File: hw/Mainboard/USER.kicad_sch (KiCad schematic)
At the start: 1 part, among them J4 USER

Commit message: hw: wip
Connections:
- net GND renamed PD_GND
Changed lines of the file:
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@@
+    (stroke (width 0) (type default) (color 0 0 0 0))
+  )
+  (wire (pts (xy 142.24 115.57) (xy 148.59 115.57))
     (stroke (width 0) (type default) (color 0 0 0 0))
   )
@@
   )
   (wire (pts (xy 167.64 85.09) (xy 167.64 86.36))
-    (stroke (width 0) (type default) (color 0 0 0 0))
-  )
-  (wire (pts (xy 142.24 115.57) (xy 148.59 115.57))
     (stroke (width 0) (type default) (color 0 0 0 0))
   )
@@
     (pin "N")
   )
-  (symbol (lib_id "power:GND") (at 115.57 86.36 0) (unit 1)
+  (symbol (lib_id "PET:PD_GND") (at 142.24 115.57 0) (unit 1)
     (in_bom yes) (on_board yes) (fields_autoplaced)
-    (property "Reference" "#PWR0117" (id 0) (at 115.57 92.71 0)
-      (effects (font (size 1.27 1.27)) hide)
-    )
-    (property "Value" "GND" (id 1) (at 115.57 91.44 0))
+    (property "Reference" "#PWR0117" (id 0) (at 142.24 121.92 0)
+      (effects (font (size 1.27 1.27)) hide)
+    )
+    (property "Value" "PD_GND" (id 1) (at 142.24 120.65 0))
+    (property "Footprint" "" (id 2) (at 142.24 115.57 0)
+      (effects (font (size 1.27 1.27)) hide)
+    )
+    (property "Datasheet" "" (id 3) (at 142.24 115.57 0)
+      (effects (font (size 1.27 1.27)) hide)
+    )
+    (pin "1")
+  )
+  (symbol (lib_id "PET:PD_GND") (at 115.57 86.36 0) (unit 1)
+    (in_bom yes) (on_board yes) (fields_autoplaced)
+    (property "Reference" "#PWR0121" (id 0) (at 115.57 92.71 0)
+      (effects (font (size 1.27 1.27)) hide)
+    )
+    (property "Value" "PD_GND" (id 1) (at 115.57 91.44 0))
     (property "Footprint" "" (id 2) (at 115.57 86.36 0)
       (effects (font (size 1.27 1.27)) hide)
@@
     (pin "1")
   )
-  (symbol (lib_id "power:GND") (at 167.64 86.36 0) (unit 1)
+  (symbol (lib_id "PET:PD_GND") (at 167.64 86.36 0) (unit 1)
     (in_bom yes) (on_board yes) (fields_autoplaced)
     (property "Reference" "#PWR0118" (id 0) (at 167.64 92.71 0)
       (effects (font (size 1.27 1.27)) hide)
     )
-    (property "Value" "GND" (id 1) (at 167.64 91.44 0))
+    (property "Value" "PD_GND" (id 1) (at 167.64 91.44 0))
     (property "Footprint" "" (id 2) (at 167.64 86.36 0)
       (effects (font (size 1.27 1.27)) hide)
@@
       (effects (font (size 1.27 1.27)) hide)
     )
-    (pin "1")
-  )
-  (symbol (lib_id "power:GND") (at 142.24 115.57 0) (unit 1)
-    (in_bom yes) (on_board yes) (fields_autoplaced)
-    (property "Reference" "#PWR0121" (id 0) (at 142.24 121.92 0)
-      (effects (font (size 1.27 1.27)) hide)
-    )
-    (property "Value" "GND" (id 1) (at 142.24 120.65 0))
-    (property "Footprint" "" (id 2) (at 142.24 115.57 0)
-      (effects (font (size 1.27 1.27)) hide)
-    )
-    (property "Datasheet" "" (id 3) (at 142.24 115.57 0)
-      (effects (font (size 1.27 1.27)) hide)
-    )

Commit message: hw: autoroute
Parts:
- added J26: USER_HEADER, Connector_PinHeader_2.54mm:PinHeader_2x11_P2.54mm_Vertical, symbol Connector_Generic:Conn_02x11_Odd_Even
- added PT26: PowerTie_2, PET:NetTie-2_SMD_Pad_1.6_to_0.4mm, symbol PET:PowerTie_2
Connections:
- net BHORIZ: now also J26.5 (Pin_5)
- net BVERT: now also J26.7 (Pin_7)
- net BVIDEO: now also J26.21 (Pin_21)
- net CASS1_READ: now also J26.9 (Pin_9)
- net CASS2_READ: now also J26.13 (Pin_13)
- net CASS_WRITE: now also J26.11 (Pin_11)
- net DIAG: now also J26.15 (Pin_15)
- net EOI: now also J26.17 (Pin_17)
- net GRAPHIC: now also J26.3 (Pin_3)
- net PD_GND: now also J26.1 (Pin_1)
- net SRQ: now also J26.19 (Pin_19)
- net VIA_CA1: now also J26.22 (Pin_22)
- net VIA_CB2: now also J26.4 (Pin_4)
- net VIA_PA0: now also J26.20 (Pin_20)
- net VIA_PA1: now also J26.18 (Pin_18)
- net VIA_PA2: now also J26.16 (Pin_16)
- net VIA_PA3: now also J26.14 (Pin_14)
- net VIA_PA4: now also J26.12 (Pin_12)
- net VIA_PA5: now also J26.10 (Pin_10)
- net VIA_PA6: now also J26.8 (Pin_8)
- net VIA_PA7: now also J26.6 (Pin_6)
- new net +5V: PT26.1
- new net VCC: J26.2 (Pin_2), PT26.2
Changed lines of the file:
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@@
     (stroke (width 0) (type default) (color 0 0 0 0))
   )
-  (wire (pts (xy 152.4 124.46) (xy 129.54 124.46))
+  (wire (pts (xy 200.66 113.03) (xy 200.66 111.76))
+    (stroke (width 0) (type default) (color 0 0 0 0))
+  )
+  (wire (pts (xy 152.4 124.46) (xy 133.35 124.46))
     (stroke (width 0) (type default) (color 0 0 0 0))
   )
@@
     (stroke (width 0) (type default) (color 0 0 0 0))
   )
+  (wire (pts (xy 213.36 111.76) (xy 218.44 111.76))
+    (stroke (width 0) (type default) (color 0 0 0 0))
+  )
   (wire (pts (xy 133.35 90.17) (xy 135.89 90.17))
     (stroke (width 0) (type default) (color 0 0 0 0))
@@
     (stroke (width 0) (type default) (color 0 0 0 0))
   )
+  (wire (pts (xy 223.52 111.76) (xy 224.79 111.76))
+    (stroke (width 0) (type default) (color 0 0 0 0))
+  )
   (wire (pts (xy 115.57 85.09) (xy 115.57 86.36))
     (stroke (width 0) (type default) (color 0 0 0 0))
@@
     (stroke (width 0) (type default) (color 0 0 0 0))
   )
+  (label "VIA_PA0" (at 213.36 88.9 0)
+    (effects (font (size 1.27 1.27)) (justify left bottom))
+  )
+  (label "VIA_PA7" (at 213.36 106.68 0)
+    (effects (font (size 1.27 1.27)) (justify left bottom))
+  )
   (label "VIA_PA1" (at 148.59 92.71 0)
     (effects (font (size 1.27 1.27)) (justify left bottom))
@@
     (effects (font (size 1.27 1.27)) (justify left bottom))
   )
+  (label "VIA_PA2" (at 213.36 93.98 0)
+    (effects (font (size 1.27 1.27)) (justify left bottom))
+  )
+  (label "VIA_PA1" (at 213.36 91.44 0)
+    (effects (font (size 1.27 1.27)) (justify left bottom))
+  )
+  (label "VIA_PA6" (at 213.36 104.14 0)
+    (effects (font (size 1.27 1.27)) (justify left bottom))
+  )
+  (label "VIA_PA4" (at 213.36 99.06 0)
+    (effects (font (size 1.27 1.27)) (justify left bottom))
+  )
+  (label "VCC" (at 218.44 111.76 180)
+    (effects (font (size 1.27 1.27)) (justify right bottom))
+  )
   (label "VIA_PA4" (at 148.59 100.33 0)
     (effects (font (size 1.27 1.27)) (justify left bottom))
   )
+  (label "VIA_PA5" (at 213.36 101.6 0)
+    (effects (font (size 1.27 1.27)) (justify left bottom))
+  )
   (label "VIA_PA6" (at 148.59 105.41 0)
     (effects (font (size 1.27 1.27)) (justify left bottom))
@@
     (effects (font (size 1.27 1.27)) (justify left bottom))
   )
+  (label "VIA_PA3" (at 213.36 96.52 0)
+    (effects (font (size 1.27 1.27)) (justify left bottom))
+  )
   (hierarchical_label "DIAG" (shape output) (at 133.35 95.25 180)
     (effects (font (size 1.27 1.27)) (justify right))
@@
     (effects (font (size 1.27 1.27)) (justify right))
   )
+  (hierarchical_label "CASS1_READ" (shape output) (at 200.66 101.6 180)
+    (effects (font (size 1.27 1.27)) (justify right))
+  )
   (hierarchical_label "VIA_PA[0..7]" (shape bidirectional) (at 129.54 71.12 180)
     (effects (font (size 1.27 1.27)) (justify right))
@@
     (effects (font (size 1.27 1.27)) (justify right))
   )
+  (hierarchical_label "CASS_WRITE" (shape input) (at 200.66 99.06 180)
+    (effects (font (size 1.27 1.27)) (justify right))
+  )
+  (hierarchical_label "BVERT" (shape input) (at 200.66 104.14 180)
+    (effects (font (size 1.27 1.27)) (justify right))
+  )
+  (hierarchical_label "EOI" (shape bidirectional) (at 200.66 91.44 180)
+    (effects (font (size 1.27 1.27)) (justify right))
+  )
   (hierarchical_label "BVIDEO" (shape input) (at 133.35 87.63 180)
     (effects (font (size 1.27 1.27)) (justify right))
   )
+  (hierarchical_label "CASS2_READ" (shape output) (at 200.66 96.52 180)
+    (effects (font (size 1.27 1.27)) (justify right))
+  )
   (hierarchical_label "VIA_CA1" (shape bidirectional) (at 129.54 73.66 180)
     (effects (font (size 1.27 1.27)) (justify right))
   )
+  (hierarchical_label "BVIDEO" (shape input) (at 200.66 86.36 180)
+    (effects (font (size 1.27 1.27)) (justify right))
+  )
   (hierarchical_label "EOI" (shape bidirectional) (at 133.35 92.71 180)
     (effects (font (size 1.27 1.27)) (justify right))
   )
-  (hierarchical_label "VIA_CB2" (shape bidirectional) (at 129.54 124.46 180)
+  (hierarchical_label "SRQ" (shape output) (at 200.66 88.9 180)
+    (effects (font (size 1.27 1.27)) (justify right))
+  )
+  (hierarchical_label "VIA_CB2" (shape bidirectional) (at 213.36 109.22 0)
+    (effects (font (size 1.27 1.27)) (justify left))
+  )
+  (hierarchical_label "VIA_CB2" (shape bidirectional) (at 133.35 124.46 180)
+    (effects (font (size 1.27 1.27)) (justify right))
+  )
+  (hierarchical_label "DIAG" (shape output) (at 200.66 93.98 180)
+    (effects (font (size 1.27 1.27)) (justify right))
+  )
+  (hierarchical_label "VIA_CA1" (shape bidirectional) (at 213.36 86.36 0)
+    (effects (font (size 1.27 1.27)) (justify left))
+  )
+  (hierarchical_label "GRAPHIC" (shape input) (at 200.66 109.22 180)
+    (effects (font (size 1.27 1.27)) (justify right))
+  )
+  (hierarchical_label "BHORIZ" (shape input) (at 200.66 106.68 180)
     (effects (font (size 1.27 1.27)) (justify right))
   )
@@
     (pin "N")
   )
+  (symbol (lib_id "Connector_Generic:Conn_02x11_Odd_Even") (at 205.74 99.06 0) (mirror x) (unit 1)
+    (in_bom yes) (on_board yes) (fields_autoplaced)
+    (property "Reference" "J26" (id 0) (at 207.01 80.01 0))
+    (property "Value" "USER_HEADER" (id 1) (at 207.01 82.55 0))
+    (property "Footprint" "Connector_PinHeader_2.54mm:PinHeader_2x11_P2.54mm_Vertical" (id 2) (at 205.74 99.06 0)
+      (effects (font (size 1.27 1.27)) hide)
+    )
+    (property "Datasheet" "~" (id 3) (at 205.74 99.06 0)
+      (effects (font (size 1.27 1.27)) hide)
+    )
+    (pin "1")
+    (pin "10")
+    (pin "11")
+    (pin "12")
+    (pin "13")
+    (pin "14")
+    (pin "15")
+    (pin "16")
+    (pin "17")
+    (pin "18")
+    (pin "19")
+    (pin "2")
+    (pin "20")
+    (pin "21")
+    (pin "22")
+    (pin "3")
+    (pin "4")
+    (pin "5")
+    (pin "6")
+    (pin "7")
+    (pin "8")
+    (pin "9")
+  )
+  (symbol (lib_id "PET:PowerTie_2") (at 220.98 111.76 180) (unit 1)
+    (in_bom yes) (on_board yes) (fields_autoplaced)
+    (property "Reference" "PT26" (id 0) (at 220.98 113.665 0)
+      (effects (font (size 1.27 1.27)) hide)
+    )
+    (property "Value" "PowerTie_2" (id 1) (at 220.98 109.855 0)
+      (effects (font (size 1.27 1.27)) hide)
+    )
+    (property "Footprint" "PET:NetTie-2_SMD_Pad_1.6_to_0.4mm" (id 2) (at 220.98 111.76 0)
+      (effects (font (size 1.27 1.27)) hide)
+    )
+    (property "Datasheet" "~" (id 3) (at 220.98 111.76 0)
+      (effects (font (size 1.27 1.27)) hide)
+    )
+    (pin "1")
+    (pin "2")
+  )
   (symbol (lib_id "PET:PD_GND") (at 142.24 115.57 0) (unit 1)
     (in_bom yes) (on_board yes) (fields_autoplaced)
@@
       (effects (font (size 1.27 1.27)) hide)
     )
+    (pin "1")
+  )
+  (symbol (lib_id "power:+5V") (at 224.79 111.76 0) (mirror x) (unit 1)
+    (in_bom yes) (on_board yes) (fields_autoplaced)
+    (property "Reference" "#PWR0188" (id 0) (at 224.79 107.95 0)
+      (effects (font (size 1.27 1.27)) hide)
+    )
+    (property "Value" "+5V" (id 1) (at 224.79 116.84 0))
+    (property "Footprint" "" (id 2) (at 224.79 111.76 0)
+      (effects (font (size 1.27 1.27)) hide)
+    )
+    (property "Datasheet" "" (id 3) (at 224.79 111.76 0)
+      (effects (font (size 1.27 1.27)) hide)
+    )
+    (pin "1")
+  )
+  (symbol (lib_id "PET:PD_GND") (at 200.66 113.03 0) (unit 1)
+    (in_bom yes) (on_board yes) (fields_autoplaced)
+    (property "Reference" "#PWR0187" (id 0) (at 200.66 119.38 0)
+      (effects (font (size 1.27 1.27)) hide)
+    )
+    (property "Value" "PD_GND" (id 1) (at 200.66 118.11 0))
+    (property "Footprint" "" (id 2) (at 200.66 113.03 0)
+      (effects (font (size 1.27 1.27)) hide)
+    )
+    (property "Datasheet" "" (id 3) (at 200.66 113.03 0)
+      (effects (font (size 1.27 1.27)) hide)
+    )

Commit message: wip
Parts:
- added JP10: VIDEO_OR_5V, Jumper:SolderJumper-3_P1.3mm_Open_RoundedPad1.0x1.5mm, symbol Jumper:SolderJumper_3_Open
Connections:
- net BVIDEO: now also JP10.1 (A); no longer J4.2 (~{VIDEO})
- net VCC: now also JP10.3 (B)
- new net VIDEO_OR_5V: J4.2 (~{VIDEO}), JP10.2 (C)
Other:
- moved on the sheet: J26, J4

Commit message: hw: add more Mouse part numbers
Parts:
- J26: MOUSER (none) -> 649-1012938195002BLF
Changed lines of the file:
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@@
+      (effects (font (size 1.27 1.27)) hide)
+    )
+    (property "MOUSER" "649-1012938195002BLF" (id 4) (at 176.53 95.25 0)
       (effects (font (size 1.27 1.27)) hide)
     )

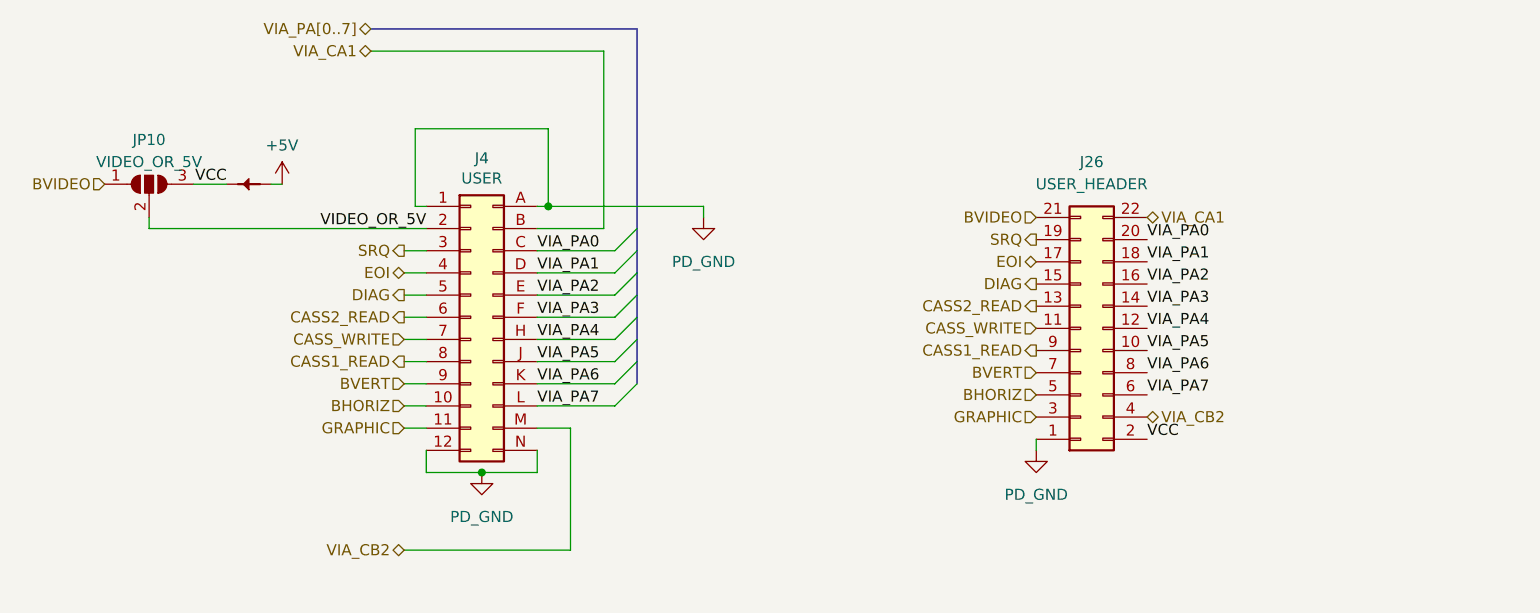
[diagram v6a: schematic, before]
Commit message: hw: 9V DC plug on left edge, change default track size
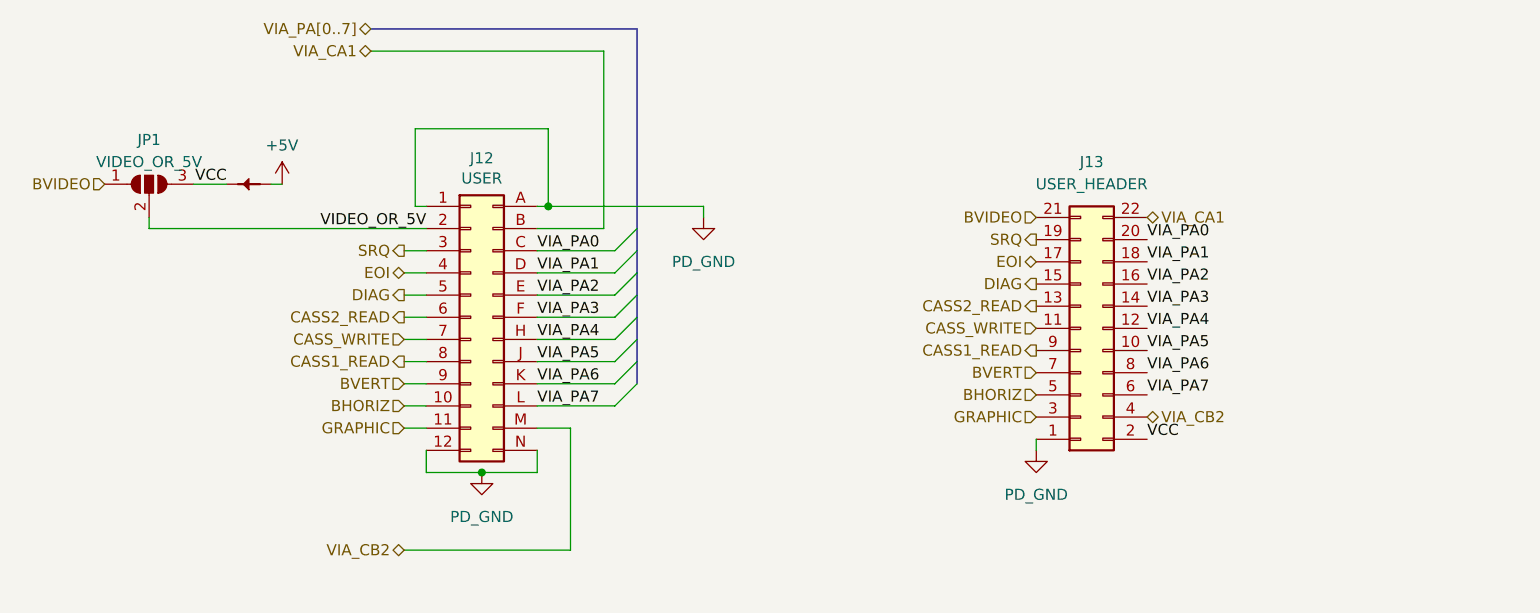
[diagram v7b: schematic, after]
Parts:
- renumbered J4 to J12, J26 to J13, JP10 to JP1, PT26 to PT37
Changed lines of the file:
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@@
   (symbol (lib_id "Retrocomputing:CBM_PET_USER_Conn_02x12_Card_Edge") (at 106.68 93.98 0) (unit 1)
     (in_bom yes) (on_board yes)
-    (property "Reference" "J4" (id 0) (at 107.95 75.7682 0))
+    (property "Reference" "J12" (id 0) (at 107.95 75.7682 0))
     (property "Value" "USER" (id 1) (at 107.95 78.0796 0))
     (property "Footprint" "Retrocomputing:CBM_PET_USER_EDGE_CON_24P" (id 2) (at 106.68 93.98 0)
@@
   (symbol (lib_id "Connector_Generic:Conn_02x11_Odd_Even") (at 176.53 95.25 0) (mirror x) (unit 1)
     (in_bom yes) (on_board yes) (fields_autoplaced)
-    (property "Reference" "J26" (id 0) (at 177.8 76.2 0))
+    (property "Reference" "J13" (id 0) (at 177.8 76.2 0))
     (property "Value" "USER_HEADER" (id 1) (at 177.8 78.74 0))
     (property "Footprint" "Connector_PinHeader_2.54mm:PinHeader_2x11_P2.54mm_Vertical" (id 2) (at 176.53 95.25 0)
@@
   (symbol (lib_id "PET:PowerTie_2") (at 81.28 78.74 180) (unit 1)
     (in_bom yes) (on_board yes) (fields_autoplaced)
-    (property "Reference" "PT26" (id 0) (at 81.28 80.645 0)
+    (property "Reference" "PT37" (id 0) (at 81.28 80.645 0)
       (effects (font (size 1.27 1.27)) hide)
     )
@@
   (symbol (lib_id "PET:PD_GND") (at 107.95 111.76 0) (unit 1)
     (in_bom yes) (on_board yes) (fields_autoplaced)
-    (property "Reference" "#PWR0117" (id 0) (at 107.95 118.11 0)
+    (property "Reference" "#PWR0105" (id 0) (at 107.95 118.11 0)
       (effects (font (size 1.27 1.27)) hide)
     )
@@
   (symbol (lib_id "PET:PD_GND") (at 133.35 82.55 0) (unit 1)
     (in_bom yes) (on_board yes) (fields_autoplaced)
-    (property "Reference" "#PWR0118" (id 0) (at 133.35 88.9 0)
+    (property "Reference" "#PWR0103" (id 0) (at 133.35 88.9 0)
       (effects (font (size 1.27 1.27)) hide)
     )
@@
   (symbol (lib_name "SolderJumper_3_Open_3") (lib_id "Jumper:SolderJumper_3_Open") (at 69.85 78.74 0) (unit 1)
     (in_bom yes) (on_board yes)
-    (property "Reference" "JP10" (id 0) (at 69.85 73.66 0))
+    (property "Reference" "JP1" (id 0) (at 69.85 73.66 0))
     (property "Value" "VIDEO_OR_5V" (id 1) (at 69.85 76.2 0))
     (property "Footprint" "Jumper:SolderJumper-3_P1.3mm_Open_RoundedPad1.0x1.5mm" (id 2) (at 69.85 78.74 0)
@@
   (symbol (lib_id "PET:PD_GND") (at 171.45 109.22 0) (unit 1)
     (in_bom yes) (on_board yes) (fields_autoplaced)
-    (property "Reference" "#PWR0187" (id 0) (at 171.45 115.57 0)
+    (property "Reference" "#PWR0104" (id 0) (at 171.45 115.57 0)
       (effects (font (size 1.27 1.27)) hide)
     )
@@
   (symbol (lib_id "power:+5V") (at 85.09 78.74 0) (mirror y) (unit 1)
     (in_bom yes) (on_board yes)
-    (property "Reference" "#PWR0121" (id 0) (at 85.09 82.55 0)
+    (property "Reference" "#PWR0102" (id 0) (at 85.09 82.55 0)
       (effects (font (size 1.27 1.27)) hide)
     )

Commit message: hw: 25x2 header (wip)
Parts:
- renumbered J12 to J13, J13 to J14
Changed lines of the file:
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@@
   (symbol (lib_id "Retrocomputing:CBM_PET_USER_Conn_02x12_Card_Edge") (at 106.68 93.98 0) (unit 1)
     (in_bom yes) (on_board yes)
-    (property "Reference" "J12" (id 0) (at 107.95 75.7682 0))
+    (property "Reference" "J13" (id 0) (at 107.95 75.7682 0))
     (property "Value" "USER" (id 1) (at 107.95 78.0796 0))
     (property "Footprint" "Retrocomputing:CBM_PET_USER_EDGE_CON_24P" (id 2) (at 106.68 93.98 0)
@@
   (symbol (lib_id "Connector_Generic:Conn_02x11_Odd_Even") (at 176.53 95.25 0) (mirror x) (unit 1)
     (in_bom yes) (on_board yes) (fields_autoplaced)
-    (property "Reference" "J13" (id 0) (at 177.8 76.2 0))
+    (property "Reference" "J14" (id 0) (at 177.8 76.2 0))
     (property "Value" "USER_HEADER" (id 1) (at 177.8 78.74 0))
     (property "Footprint" "Connector_PinHeader_2.54mm:PinHeader_2x11_P2.54mm_Vertical" (id 2) (at 176.53 95.25 0)
@@
   (symbol (lib_id "PET:PD_GND") (at 107.95 111.76 0) (unit 1)
     (in_bom yes) (on_board yes) (fields_autoplaced)
-    (property "Reference" "#PWR0105" (id 0) (at 107.95 118.11 0)
+    (property "Reference" "#PWR0107" (id 0) (at 107.95 118.11 0)
       (effects (font (size 1.27 1.27)) hide)
     )
@@
   (symbol (lib_id "PET:PD_GND") (at 133.35 82.55 0) (unit 1)
     (in_bom yes) (on_board yes) (fields_autoplaced)
-    (property "Reference" "#PWR0103" (id 0) (at 133.35 88.9 0)
+    (property "Reference" "#PWR0105" (id 0) (at 133.35 88.9 0)
       (effects (font (size 1.27 1.27)) hide)
     )
@@
   (symbol (lib_id "PET:PD_GND") (at 171.45 109.22 0) (unit 1)
     (in_bom yes) (on_board yes) (fields_autoplaced)
-    (property "Reference" "#PWR0104" (id 0) (at 171.45 115.57 0)
+    (property "Reference" "#PWR0106" (id 0) (at 171.45 115.57 0)
       (effects (font (size 1.27 1.27)) hide)
     )
@@
   (symbol (lib_id "power:+5V") (at 85.09 78.74 0) (mirror y) (unit 1)
     (in_bom yes) (on_board yes)
-    (property "Reference" "#PWR0102" (id 0) (at 85.09 82.55 0)
+    (property "Reference" "#PWR0104" (id 0) (at 85.09 82.55 0)
       (effects (font (size 1.27 1.27)) hide)
     )
